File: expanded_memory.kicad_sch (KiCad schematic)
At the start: 7 parts, among them U14 74HC02, U16 AS6C4008-55PCN, U17 AS6C4008-55PCN, U18 74LS244, U19 74AHC1G86, U7 74HC04, U8 74HC00

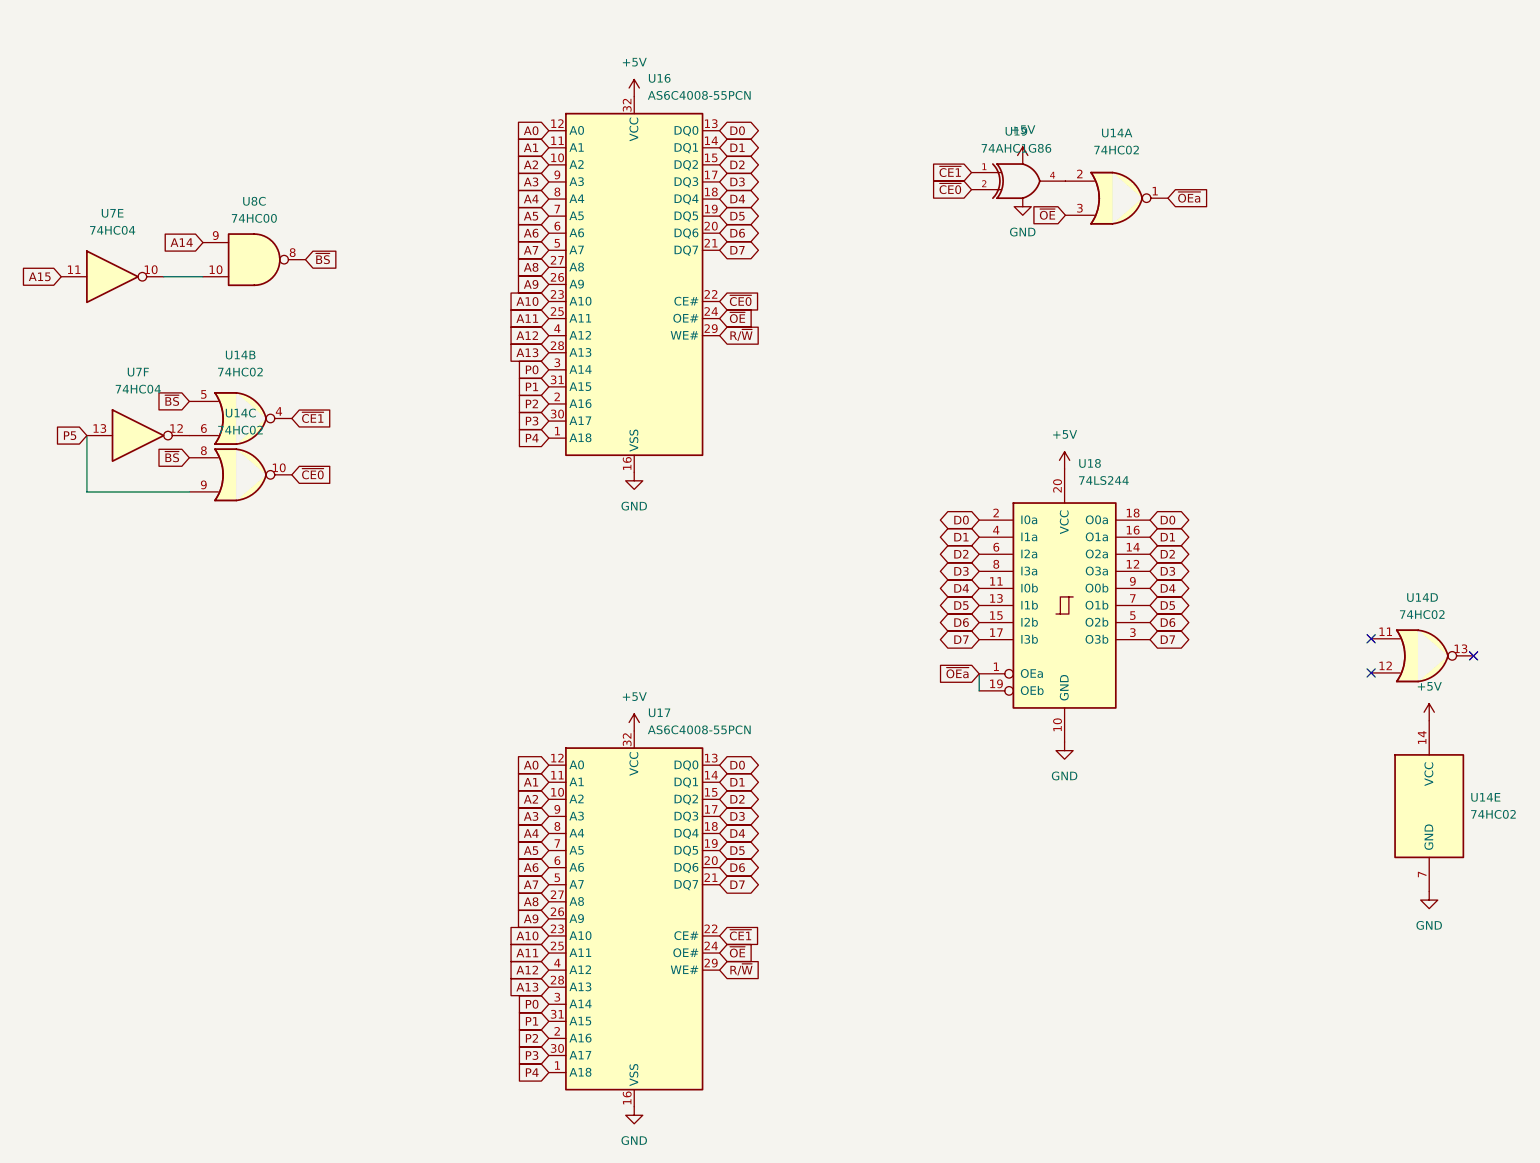
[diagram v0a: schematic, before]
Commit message: add power routing
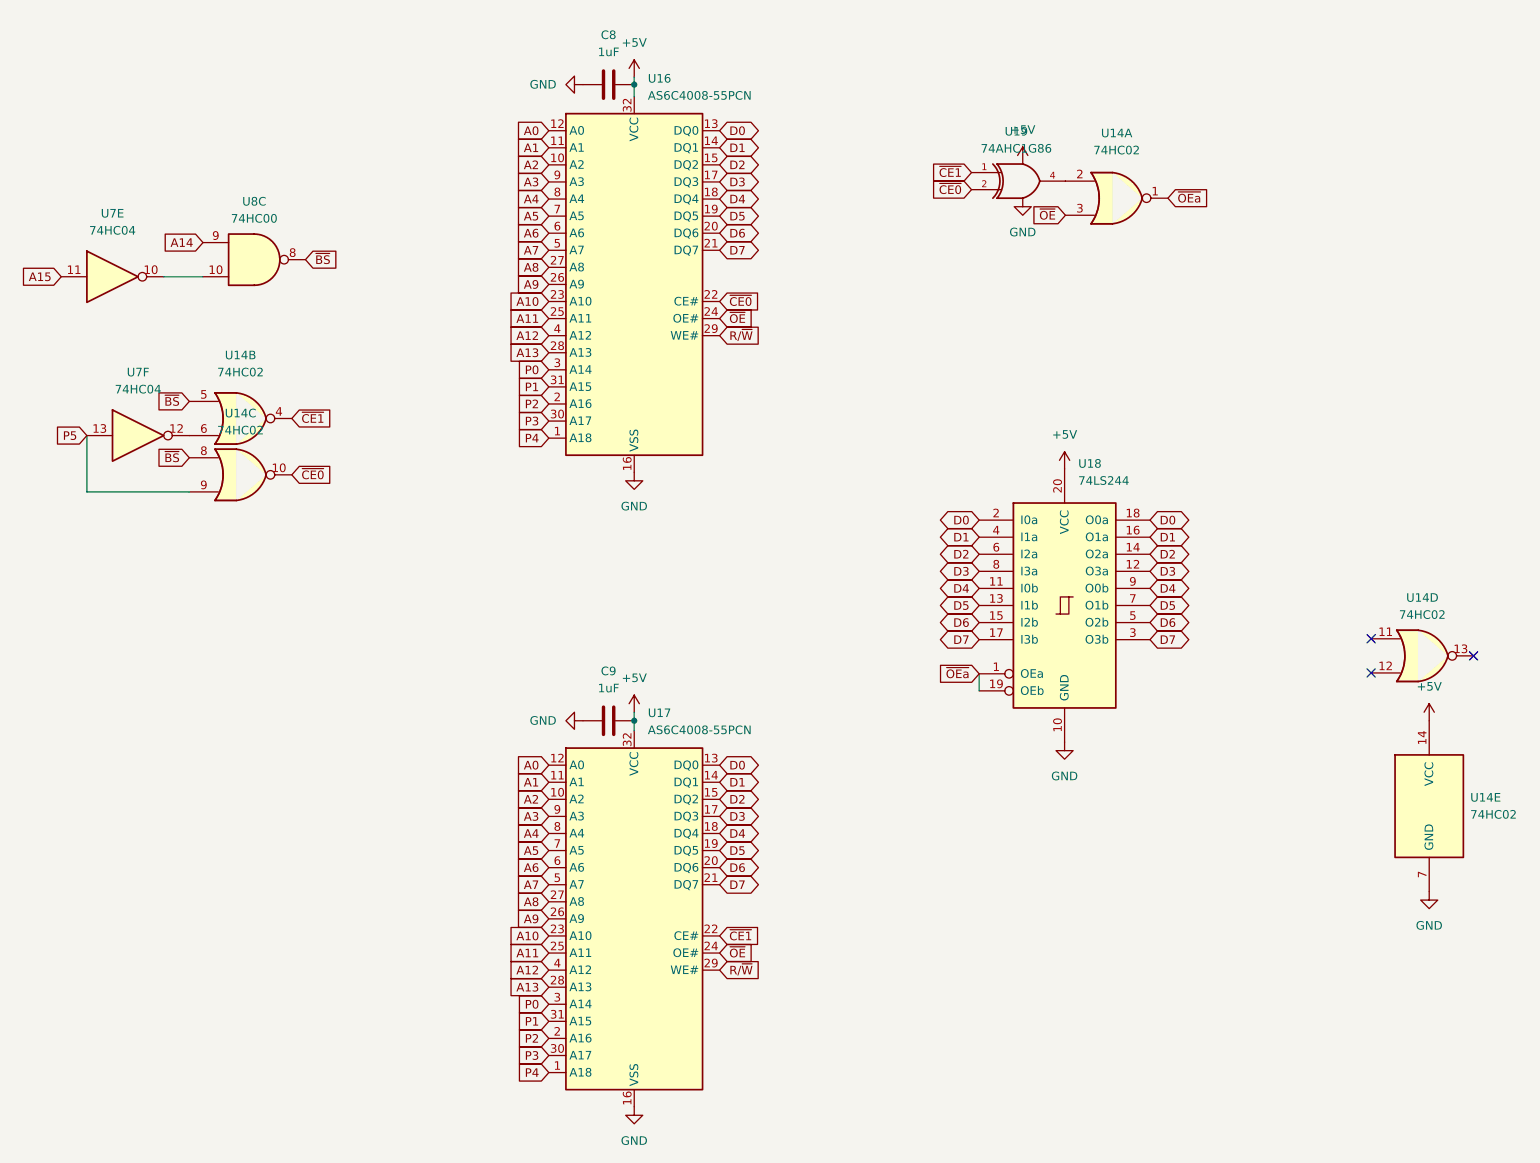
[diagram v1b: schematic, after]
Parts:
- added C8, C9: 1uF, Capacitor_SMD:C_0805_2012Metric, symbol Device:C
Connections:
- net +5V: now also C8.1, C9.1
- net GND: now also C8.2, C9.2

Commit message: reduce component count
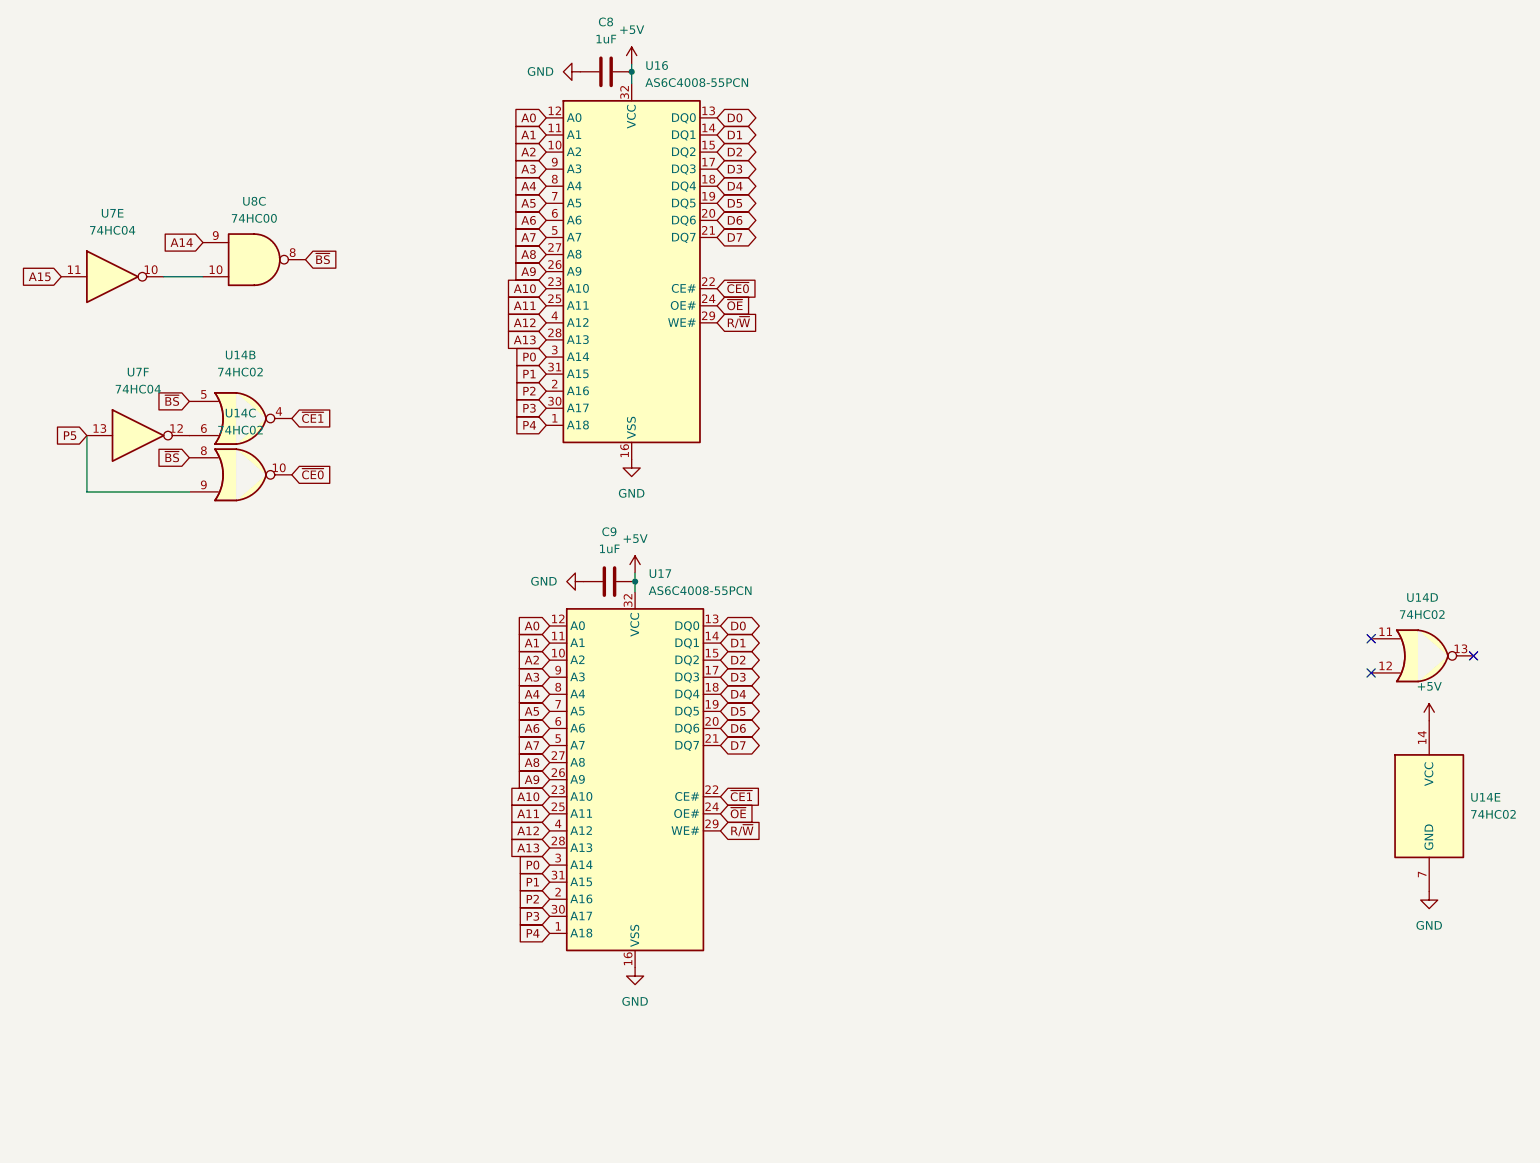
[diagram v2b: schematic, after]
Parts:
- removed unit 1 of U14
- removed U18: 74LS244, Package_SO:SO-20_5.3x12.6mm_P1.27mm, symbol 74xx:74LS244
- removed U19: 74AHC1G86, Package_SO:TSOP-5_1.65x3.05mm_P0.95mm, symbol 74xGxx:74AHC1G86
- U16, U17: footprint Package_SO:TSOP-I-32_18.4x8mm_P0.5mm -> Package_SO:SSOP-32_11.305x20.495mm_P1.27mm
